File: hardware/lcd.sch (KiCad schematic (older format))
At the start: 3 parts

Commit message: Die 3 Taster müssen auf GND liegen und nich auf +5V ! Es werden die internen PullUps des µC verwendet.
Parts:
- RV1: symbol POT -> POT-RESCUE-1541-rebuild
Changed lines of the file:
@@
 EESchema Schematic File Version 2
+LIBS:1541-rebuild-rescue
 LIBS:power
 LIBS:device
@@
 	5450 3350 5450 3500
 $Comp
-L POT RV1
+L POT-RESCUE-1541-rebuild RV1
 U 1 1 55F9F8C0
 P 5000 3400

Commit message: diverese Sachen geändert
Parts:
- DS1: footprint Display:WC1602A -> Pin_Headers:Pin_Header_Straight_1x16
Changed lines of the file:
@@
 	6850 3350 6850 3500
 $Comp
-L GND #PWR012
+L GND #PWR015
 U 1 1 55F9D0E8
 P 6850 3500
-F 0 "#PWR012" H 6850 3250 50  0001 C CNN
+F 0 "#PWR015" H 6850 3250 50  0001 C CNN
 F 1 "GND" H 6850 3350 50  0000 C CNN
 F 2 "" H 6850 3500 60  0000 C CNN
@@
 F 0 "DS1" H 5300 3250 40  0000 C CNN
 F 1 "LCD16X2" H 6800 3250 40  0000 C CNN
-F 2 "Display:WC1602A" H 6100 2800 35  0000 C CIN
+F 2 "Pin_Headers:Pin_Header_Straight_1x16" H 6100 2800 35  0000 C CIN
 F 3 "" H 6100 2850 60  0000 C CNN
 	1    6100 2850
@@
 Connection ~ 5750 3400
 $Comp
-L +5V #PWR013
+L +5V #PWR016
 U 1 1 55F9F555
 P 5450 3500
-F 0 "#PWR013" H 5450 3350 50  0001 C CNN
+F 0 "#PWR016" H 5450 3350 50  0001 C CNN
 F 1 "+5V" H 5450 3640 50  0000 C CNN
 F 2 "" H 5450 3500 60  0000 C CNN
@@
 	5550 3750 5550 3350
 $Comp
-L +5V #PWR014
+L +5V #PWR017
 U 1 1 55F9F9A0
 P 4650 3400
-F 0 "#PWR014" H 4650 3250 50  0001 C CNN
+F 0 "#PWR017" H 4650 3250 50  0001 C CNN
 F 1 "+5V" H 4650 3540 50  0000 C CNN
 F 2 "" H 4650 3400 60  0000 C CNN
@@
 $EndComp
 $Comp
-L +5V #PWR015
+L +5V #PWR018
 U 1 1 55F9FC92
 P 6750 4100
-F 0 "#PWR015" H 6750 3950 50  0001 C CNN
+F 0 "#PWR018" H 6750 3950 50  0001 C CNN
 F 1 "+5V" H 6750 4240 50  0000 C CNN
 F 2 "" H 6750 4100 60  0000 C CNN

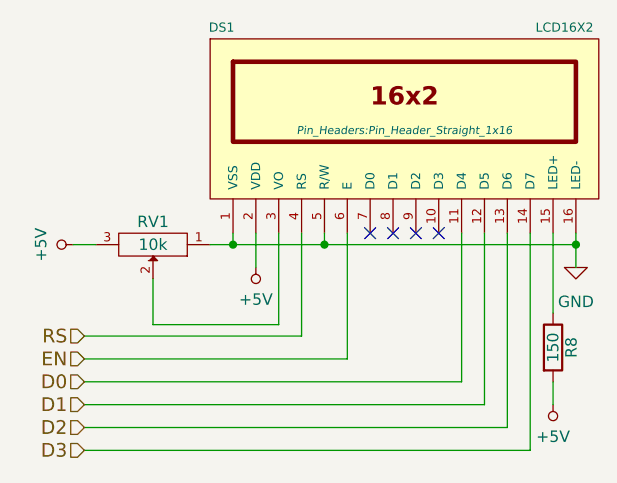
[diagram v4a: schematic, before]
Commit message: Platine per Autorouter geroutet.
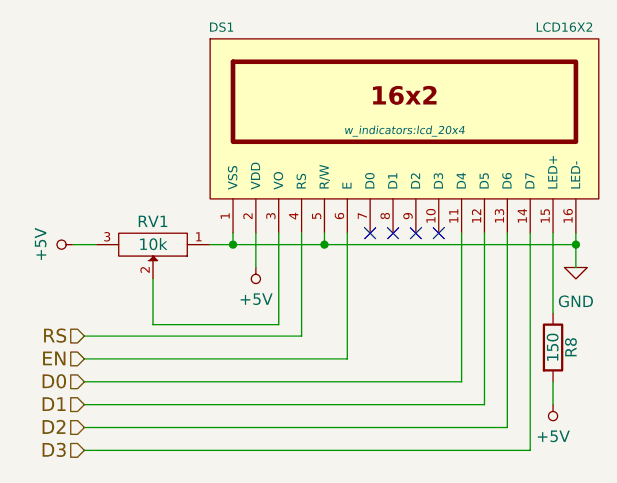
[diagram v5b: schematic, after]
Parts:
- DS1: footprint Pin_Headers:Pin_Header_Straight_1x16 -> w_indicators:lcd_20x4
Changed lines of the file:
@@
 LIBS:valves
 LIBS:Oscillators
+LIBS:w_analog
+LIBS:w_connectors
+LIBS:w_device
+LIBS:w_logic
+LIBS:w_memory
+LIBS:w_microcontrollers
+LIBS:w_opto
+LIBS:w_relay
+LIBS:w_rtx
+LIBS:w_transistor
+LIBS:w_vacuum
 LIBS:1541-rebuild-cache
 EELAYER 25 0
@@
 F 0 "DS1" H 5300 3250 40  0000 C CNN
 F 1 "LCD16X2" H 6800 3250 40  0000 C CNN
-F 2 "Pin_Headers:Pin_Header_Straight_1x16" H 6100 2800 35  0000 C CIN
+F 2 "w_indicators:lcd_20x4" H 6100 2800 35  0000 C CIN
 F 3 "" H 6100 2850 60  0000 C CNN
 	1    6100 2850

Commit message: Debug LED im Schaltplan eingefügt.
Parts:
- renumbered R8 to R9
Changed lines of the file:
@@
 encoding utf-8
 Sheet 3 4
-Title "1541-rebuild"
-Date "2015-09-16"
-Rev "1.0"
+Title "1541-rebuid"
+Date "2018-04-18"
+Rev "1.1"
 Comp ""
-Comment1 "Erstellt von: Thorsten Kattanek"
+Comment1 "Erstellt: von: Thorsten Kattanek"
 Comment2 ""
 Comment3 ""
@@
 	6850 3350 6850 3500
 $Comp
-L GND #PWR015
+L GND #PWR19
 U 1 1 55F9D0E8
 P 6850 3500
-F 0 "#PWR015" H 6850 3250 50  0001 C CNN
+F 0 "#PWR19" H 6850 3250 50  0001 C CNN
 F 1 "GND" H 6850 3350 50  0000 C CNN
 F 2 "" H 6850 3500 60  0000 C CNN
@@
 Connection ~ 5750 3400
 $Comp
-L +5V #PWR016
+L +5V #PWR17
 U 1 1 55F9F555
 P 5450 3500
-F 0 "#PWR016" H 5450 3350 50  0001 C CNN
+F 0 "#PWR17" H 5450 3350 50  0001 C CNN
 F 1 "+5V" H 5450 3640 50  0000 C CNN
 F 2 "" H 5450 3500 60  0000 C CNN
@@
 	5550 3750 5550 3350
 $Comp
-L +5V #PWR017
+L +5V #PWR16
 U 1 1 55F9F9A0
 P 4650 3400
-F 0 "#PWR017" H 4650 3250 50  0001 C CNN
+F 0 "#PWR16" H 4650 3250 50  0001 C CNN
 F 1 "+5V" H 4650 3540 50  0000 C CNN
 F 2 "" H 4650 3400 60  0000 C CNN
@@
 	4650 3400 4750 3400
 $Comp
-L R R8
+L R R9
 U 1 1 55F9FBFA
 P 6750 3850
-F 0 "R8" V 6830 3850 50  0000 C CNN
+F 0 "R9" V 6830 3850 50  0000 C CNN
 F 1 "150" V 6750 3850 50  0000 C CNN
 F 2 "Resistors_ThroughHole:Resistor_Horizontal_RM10mm" V 6680 3850 30  0001 C CNN
@@
 $EndComp
 $Comp
-L +5V #PWR018
+L +5V #PWR18
 U 1 1 55F9FC92
 P 6750 4100
-F 0 "#PWR018" H 6750 3950 50  0001 C CNN
+F 0 "#PWR18" H 6750 3950 50  0001 C CNN
 F 1 "+5V" H 6750 4240 50  0000 C CNN
 F 2 "" H 6750 4100 60  0000 C CNN

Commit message: Änderungen am Schaltplan: - Resettaster eingefügt - SD Card Slot -> WP und DETECT richtig angeschlossen - auf Version 1.2 hochgesetzt
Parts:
- renumbered R9 to R11
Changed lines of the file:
@@
 Sheet 3 4
 Title "1541-rebuid"
-Date "2018-04-18"
-Rev "1.1"
+Date "2018-04-21"
+Rev "1.2"
 Comp ""
 Comment1 "Erstellt: von: Thorsten Kattanek"
@@
 	6850 3350 6850 3500
 $Comp
-L GND #PWR19
+L GND #PWR20
 U 1 1 55F9D0E8
 P 6850 3500
-F 0 "#PWR19" H 6850 3250 50  0001 C CNN
+F 0 "#PWR20" H 6850 3250 50  0001 C CNN
 F 1 "GND" H 6850 3350 50  0000 C CNN
 F 2 "" H 6850 3500 60  0000 C CNN
@@
 Connection ~ 5750 3400
 $Comp
-L +5V #PWR17
+L +5V #PWR18
 U 1 1 55F9F555
 P 5450 3500
-F 0 "#PWR17" H 5450 3350 50  0001 C CNN
+F 0 "#PWR18" H 5450 3350 50  0001 C CNN
 F 1 "+5V" H 5450 3640 50  0000 C CNN
 F 2 "" H 5450 3500 60  0000 C CNN
@@
 	5550 3750 5550 3350
 $Comp
-L +5V #PWR16
+L +5V #PWR17
 U 1 1 55F9F9A0
 P 4650 3400
-F 0 "#PWR16" H 4650 3250 50  0001 C CNN
+F 0 "#PWR17" H 4650 3250 50  0001 C CNN
 F 1 "+5V" H 4650 3540 50  0000 C CNN
 F 2 "" H 4650 3400 60  0000 C CNN
@@
 	4650 3400 4750 3400
 $Comp
-L R R9
+L R R11
 U 1 1 55F9FBFA
 P 6750 3850
-F 0 "R9" V 6830 3850 50  0000 C CNN
+F 0 "R11" V 6830 3850 50  0000 C CNN
 F 1 "150" V 6750 3850 50  0000 C CNN
 F 2 "Resistors_ThroughHole:Resistor_Horizontal_RM10mm" V 6680 3850 30  0001 C CNN
@@
 $EndComp
 $Comp
-L +5V #PWR18
+L +5V #PWR19
 U 1 1 55F9FC92
 P 6750 4100
-F 0 "#PWR18" H 6750 3950 50  0001 C CNN
+F 0 "#PWR19" H 6750 3950 50  0001 C CNN
 F 1 "+5V" H 6750 4240 50  0000 C CNN
 F 2 "" H 6750 4100 60  0000 C CNN
